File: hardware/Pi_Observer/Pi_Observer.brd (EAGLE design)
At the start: 101.6 x 64.4 mm, 17 parts, among them Q1 BC548B, U1 DS18B20, U2 DS18B20, X1 RASPI_GPIO_B+#_PIN

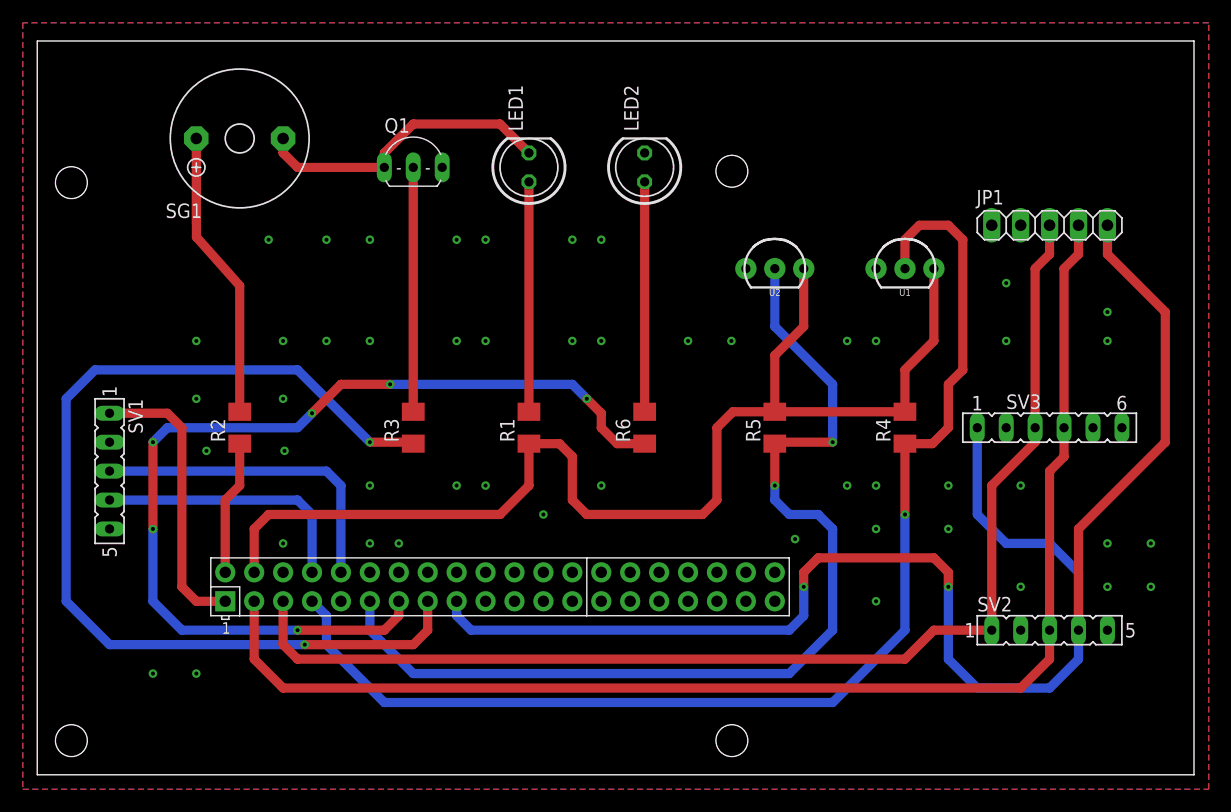
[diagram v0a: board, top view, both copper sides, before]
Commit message: Fix pcb orientation
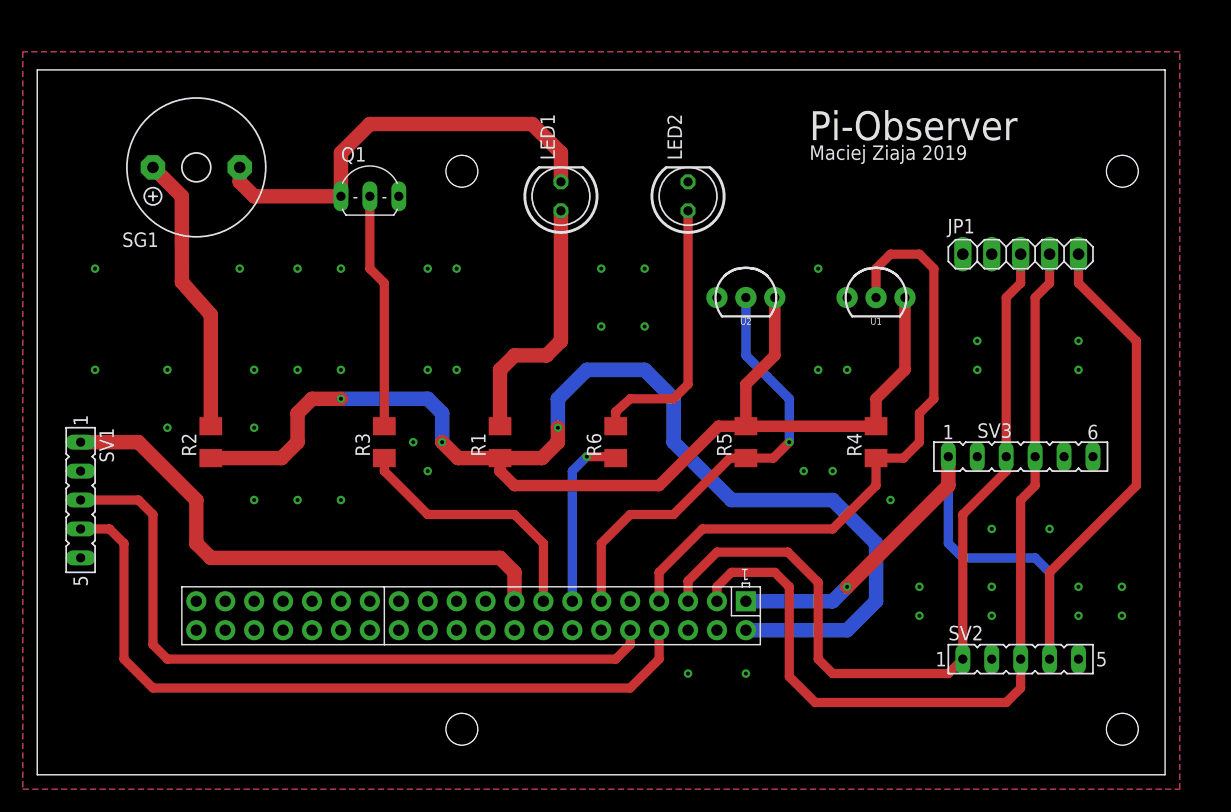
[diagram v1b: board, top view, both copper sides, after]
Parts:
- moved Q1 4.58 mm to (29.2, 52.1)
- moved LED2 4.58 mm to (57.1, 50.8)
- moved SG1 4.58 mm to (14.0, 53.3)
- moved LED1 3.79 mm to (46.0, 50.8)
- moved U1 3.59 mm to (73.7, 41.9)
- moved JP1 3.59 mm to (86.4, 45.7)
- moved SV2 3.59 mm to (86.4, 10.2)
- moved SV3 3.59 mm to (86.4, 27.9)
- moved U2 3.59 mm to (62.2, 41.9)
- moved SV1 3.59 mm to (3.81, 24.1)
- moved X1 3.59 mm to (38.1, 14.0), turned to 180 degrees
- moved R4 2.84 mm to (73.7, 29.2)
- moved R6 2.84 mm to (50.8, 29.2)
- moved R3 2.84 mm to (30.5, 29.2)
- moved R2 2.84 mm to (15.2, 29.2)
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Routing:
- net GPIO27: track 86.6 -> 15.8 mm, vias 6 -> 1
- net GPIO22: track 88.4 -> 23.0 mm, vias 2 -> 0
- net GPIO04: track 106.3 -> 56.0 mm, vias 1 -> 0
- net GPIO17: track 88.8 -> 39.6 mm, vias 2 -> 1
- net TX: track 23.4 -> 66.1 mm
- net +5V: track 117.7 -> 159.0 mm, vias 0 -> 3
- net SDA: track 116.2 -> 77.5 mm
- net RX: track 28.5 -> 62.5 mm
- net SCL: track 105.3 -> 73.5 mm
- net +3V3: track 163.8 -> 138.1 mm, vias 2 -> 1
- net N$1: track 26.8 -> 38.5 mm
- net N$9: track 20.2 -> 23.8 mm
- net N$3: track 20.2 -> 22.8 mm
- net N$5: track 21.5 -> 20.7 mm
- net N$2: track 25.4 -> 24.7 mm
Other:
- board size 101.6 x 64.4 mm -> 99 x 61.9 mm
- board text added: "Maciej Ziaja 2019"
- board text added: "Pi-Observer"
